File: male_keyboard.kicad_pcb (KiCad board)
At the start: 2 copper layers, 1 part, among them J1 Elite-Pi Microcontroller

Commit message: 1504202502
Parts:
- added J2: AudioJack4, Keebio-Parts:TRRS-PJ-320A, F.Cu at (34.8, 87.3)
- added SW1: SW_MEC_5G, Button_Switch_Keyboard:SW_Cherry_MX_1.00u_PCB, F.Cu at (101.5, 22.4)
- moved J1 36.6 mm to (64.5, 56.8)
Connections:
- J1 pad 19: unconnected-(J1-Pin_19-Pad19) -> Net-(J1-Pin_19)
- J1 pad 2: GND -> Net-(J1-Pin_2)
- J1 pad 21: unconnected-(J1-Pin_21-Pad21) -> Net-(J1-Pin_21)
- J1 pad 23: unconnected-(J1-Pin_23-Pad23) -> GND

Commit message: Label controller
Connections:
- net Net-(J1-Pin_21) renamed VCC
- J1 pad 1: unconnected-(J1-Pin_1-Pad1) -> 1
- J1 pad 10: unconnected-(J1-Pin_10-Pad10) -> 8
- J1 pad 11: unconnected-(J1-Pin_11-Pad11) -> 9
- J1 pad 12: unconnected-(J1-Pin_12-Pad12) -> 10
- J1 pad 13: unconnected-(J1-Pin_13-Pad13) -> 15
- J1 pad 14: unconnected-(J1-Pin_14-Pad14) -> 16
- J1 pad 15: unconnected-(J1-Pin_15-Pad15) -> 17
- J1 pad 16: unconnected-(J1-Pin_16-Pad16) -> 18
- J1 pad 19: Net-(J1-Pin_19) -> unconnected-(J1-Pin_19-Pad19)
- J1 pad 2: Net-(J1-Pin_2) -> 2
- J1 pad 25: unconnected-(J1-Pin_25-Pad25) -> 10
- J1 pad 26: unconnected-(J1-Pin_26-Pad26) -> 11
- J1 pad 27: unconnected-(J1-Pin_27-Pad27) -> 12
- J1 pad 28: unconnected-(J1-Pin_28-Pad28) -> 13
- J1 pad 29: unconnected-(J1-Pin_29-Pad29) -> 14
- J1 pad 3: unconnected-(J1-Pin_3-Pad3) -> GND
- J1 pad 4: unconnected-(J1-Pin_4-Pad4) -> GND
- J1 pad 5: unconnected-(J1-Pin_5-Pad5) -> 3
- J1 pad 6: unconnected-(J1-Pin_6-Pad6) -> 4
- J1 pad 7: unconnected-(J1-Pin_7-Pad7) -> 5
- J1 pad 8: unconnected-(J1-Pin_8-Pad8) -> 6
- J1 pad 9: unconnected-(J1-Pin_9-Pad9) -> 7
- J2 pad 3: Net-(J1-Pin_2) -> R1
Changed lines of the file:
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@@
 			(psa4output no)
 			(plot_black_and_white yes)
-			(plotinvisibletext no)
 			(sketchpadsonfab no)
 			(plotpadnumbers no)
@@
 	)
 	(net 0 "")
-	(net 1 "unconnected-(J1-Pin_6-Pad6)")
-	(net 2 "unconnected-(J1-Pin_15-Pad15)")
-	(net 3 "unconnected-(J1-Pin_26-Pad26)")
-	(net 4 "unconnected-(J1-Pin_28-Pad28)")
-	(net 5 "unconnected-(J1-Pin_13-Pad13)")
-	(net 6 "Net-(J1-Pin_21)")
-	(net 7 "unconnected-(J1-Pin_12-Pad12)")
-	(net 8 "unconnected-(J1-Pin_8-Pad8)")
+	(net 1 "4")
+	(net 2 "17")
+	(net 3 "11")
+	(net 4 "13")
+	(net 5 "15")
+	(net 6 "10")
+	(net 7 "6")
+	(net 8 "1")
 	(net 9 "unconnected-(J1-Pin_17-Pad17)")
-	(net 10 "unconnected-(J1-Pin_1-Pad1)")
-	(net 11 "unconnected-(J1-Pin_16-Pad16)")
-	(net 12 "unconnected-(J1-Pin_3-Pad3)")
-	(net 13 "unconnected-(J1-Pin_9-Pad9)")
-	(net 14 "unconnected-(J1-Pin_25-Pad25)")
-	(net 15 "Net-(J1-Pin_2)")
-	(net 16 "unconnected-(J1-Pin_5-Pad5)")
-	(net 17 "unconnected-(J1-Pin_14-Pad14)")
-	(net 18 "unconnected-(J1-Pin_11-Pad11)")
-	(net 19 "unconnected-(J1-Pin_7-Pad7)")
-	(net 20 "unconnected-(J1-Pin_10-Pad10)")
-	(net 21 "unconnected-(J1-Pin_4-Pad4)")
-	(net 22 "unconnected-(J1-Pin_29-Pad29)")
+	(net 10 "18")
+	(net 11 "7")
+	(net 12 "VCC")
+	(net 13 "3")
+	(net 14 "16")
+	(net 15 "9")
+	(net 16 "5")
+	(net 17 "8")
+	(net 18 "14")
+	(net 19 "2")
+	(net 20 "unconnected-(J1-Pin_19-Pad19)")
+	(net 21 "12")
+	(net 22 "R1")
 	(net 23 "unconnected-(J1-Pin_24-Pad24)")
 	(net 24 "unconnected-(J1-Pin_18-Pad18)")
@@
 	(net 26 "unconnected-(J1-Pin_20-Pad20)")
 	(net 27 "unconnected-(J1-Pin_22-Pad22)")
-	(net 28 "unconnected-(J1-Pin_27-Pad27)")
-	(net 29 "GND")
+	(net 28 "GND")
 	(footprint "Button_Switch_Keyboard:SW_Cherry_MX_1.00u_PCB"
 		(layer "F.Cu")
@@
 			(layers "*.Cu" "*.Mask")
 			(remove_unused_layers no)
-			(net 29 "GND")
+			(net 28 "GND")
 			(pinfunction "2")
 			(pintype "passive")
@@
 			(layers "*.Cu" "*.SilkS" "*.Mask")
 			(remove_unused_layers no)
-			(net 10 "unconnected-(J1-Pin_1-Pad1)")
+			(net 8 "1")
 			(pinfunction "Pin_1")
 			(pintype "passive")
@@
 			(layers "*.Cu" "*.SilkS" "*.Mask")
 			(remove_unused_layers no)
-			(net 15 "Net-(J1-Pin_2)")
+			(net 19 "2")
 			(pinfunction "Pin_2")
 			(pintype "passive")
@@
 			(layers "*.Cu" "*.SilkS" "*.Mask")
 			(remove_unused_layers no)
-			(net 12 "unconnected-(J1-Pin_3-Pad3)")
+			(net 28 "GND")
 			(pinfunction "Pin_3")
 			(pintype "passive")
@@
 			(layers "*.Cu" "*.SilkS" "*.Mask")
 			(remove_unused_layers no)
-			(net 21 "unconnected-(J1-Pin_4-Pad4)")
+			(net 28 "GND")
 			(pinfunction "Pin_4")
 			(pintype "passive")
@@
 			(layers "*.Cu" "*.SilkS" "*.Mask")
 			(remove_unused_layers no)
-			(net 16 "unconnected-(J1-Pin_5-Pad5)")
+			(net 13 "3")
 			(pinfunction "Pin_5")
 			(pintype "passive")
@@
 			(layers "*.Cu" "*.SilkS" "*.Mask")
 			(remove_unused_layers no)
-			(net 1 "unconnected-(J1-Pin_6-Pad6)")
+			(net 1 "4")
 			(pinfunction "Pin_6")
 			(pintype "passive")
@@
 			(layers "*.Cu" "*.SilkS" "*.Mask")
 			(remove_unused_layers no)
-			(net 19 "unconnected-(J1-Pin_7-Pad7)")
+			(net 16 "5")
 			(pinfunction "Pin_7")
 			(pintype "passive")
@@
 			(layers "*.Cu" "*.SilkS" "*.Mask")
 			(remove_unused_layers no)
-			(net 8 "unconnected-(J1-Pin_8-Pad8)")
+			(net 7 "6")
 			(pinfunction "Pin_8")
 			(pintype "passive")
@@
 			(layers "*.Cu" "*.SilkS" "*.Mask")
 			(remove_unused_layers no)
-			(net 13 "unconnected-(J1-Pin_9-Pad9)")
+			(net 11 "7")
 			(pinfunction "Pin_9")
 			(pintype "passive")
@@
 			(layers "*.Cu" "*.SilkS" "*.Mask")
 			(remove_unused_layers no)
-			(net 20 "unconnected-(J1-Pin_10-Pad10)")
+			(net 17 "8")
 			(pinfunction "Pin_10")
 			(pintype "passive")
@@
 			(layers "*.Cu" "*.SilkS" "*.Mask")
 			(remove_unused_layers no)
-			(net 18 "unconnected-(J1-Pin_11-Pad11)")
+			(net 15 "9")
 			(pinfunction "Pin_11")
 			(pintype "passive")
@@
 			(layers "*.Cu" "*.SilkS" "*.Mask")
 			(remove_unused_layers no)
-			(net 7 "unconnected-(J1-Pin_12-Pad12)")
+			(net 6 "10")
 			(pinfunction "Pin_12")
 			(pintype "passive")
@@
 			(layers "*.Cu" "*.SilkS" "*.Mask")
 			(remove_unused_layers no)
-			(net 5 "unconnected-(J1-Pin_13-Pad13)")
+			(net 5 "15")
 			(pinfunction "Pin_13")
 			(pintype "passive")
@@
 			(layers "*.Cu" "*.SilkS" "*.Mask")
 			(remove_unused_layers no)
-			(net 17 "unconnected-(J1-Pin_14-Pad14)")
+			(net 14 "16")
 			(pinfunction "Pin_14")
 			(pintype "passive")
@@
 			(layers "*.Cu" "*.SilkS" "*.Mask")
 			(remove_unused_layers no)
-			(net 2 "unconnected-(J1-Pin_15-Pad15)")
+			(net 2 "17")
 			(pinfunction "Pin_15")
 			(pintype "passive")
@@
 			(layers "*.Cu" "*.SilkS" "*.Mask")
 			(remove_unused_layers no)
-			(net 11 "unconnected-(J1-Pin_16-Pad16)")
+			(net 10 "18")
 			(pinfunction "Pin_16")
 			(pintype "passive")
@@
 			(layers "*.Cu" "*.SilkS" "*.Mask")
 			(remove_unused_layers no)
-			(net 25 "Net-(J1-Pin_19)")
+			(net 20 "unconnected-(J1-Pin_19-Pad19)")
 			(pinfunction "Pin_19")
 			(pintype "passive")
@@
 			(layers "*.Cu" "*.SilkS" "*.Mask")
 			(remove_unused_layers no)
-			(net 6 "Net-(J1-Pin_21)")
+			(net 12 "VCC")
 			(pinfunction "Pin_21")
 			(pintype "passive")
@@
 			(layers "*.Cu" "*.SilkS" "*.Mask")
 			(remove_unused_layers no)
-			(net 29 "GND")
+			(net 28 "GND")
 			(pinfunction "Pin_23")
 			(pintype "passive")
@@
 			(layers "*.Cu" "*.SilkS" "*.Mask")
 			(remove_unused_layers no)
-			(net 14 "unconnected-(J1-Pin_25-Pad25)")
+			(net 6 "10")
 			(pinfunction "Pin_25")
 			(pintype "passive")
@@
 			(layers "*.Cu" "*.SilkS" "*.Mask")
 			(remove_unused_layers no)
-			(net 3 "unconnected-(J1-Pin_26-Pad26)")
+			(net 3 "11")
 			(pinfunction "Pin_26")
 			(pintype "passive")
@@
 			(layers "*.Cu" "*.SilkS" "*.Mask")
 			(remove_unused_layers no)
-			(net 28 "unconnected-(J1-Pin_27-Pad27)")
+			(net 21 "12")
 			(pinfunction "Pin_27")
 			(pintype "passive")
@@
 			(layers "*.Cu" "*.SilkS" "*.Mask")
 			(remove_unused_layers no)
-			(net 4 "unconnected-(J1-Pin_28-Pad28)")
+			(net 4 "13")
 			(pinfunction "Pin_28")
 			(pintype "passive")
@@
 			(layers "*.Cu" "*.SilkS" "*.Mask")
 			(remove_unused_layers no)
-			(net 22 "unconnected-(J1-Pin_29-Pad29)")
+			(net 18 "14")
 			(pinfunction "Pin_29")
 			(pintype "passive")
@@
 			(layers "*.Cu" "*.Mask")
 			(remove_unused_layers no)
-			(net 29 "GND")
+			(net 28 "GND")
 			(pintype "passive")
 		)
@@
 			(layers "*.Cu" "*.Mask")
 			(remove_unused_layers no)
-			(net 29 "GND")
+			(net 28 "GND")
 			(pintype "passive")
 		)
@@
 			(layers "*.Cu" "*.Mask")
 			(remove_unused_layers no)
-			(net 15 "Net-(J1-Pin_2)")
+			(net 22 "R1")
 			(pintype "passive")
 		)
@@
 			(layers "*.Cu" "*.Mask")
 			(remove_unused_layers no)
-			(net 6 "Net-(J1-Pin_21)")
-			(pintype "passive")
-		)
+			(net 12 "VCC")
+			(pintype "passive")
+		)

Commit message: sort pcb
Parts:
- added J3: AudioJack4, Keebio-Parts:TRRS-PJ-320A, F.Cu at (160.9, 93.1)
- added J4: Elite-Pi Microcontroller, Keebio-Parts:Elite-C, F.Cu at (166.6, 70.9)
- added SW10: SW_Push, Button_Switch_Keyboard:SW_Cherry_MX_1.00u_PCB, F.Cu at (112.8, 81.5)
- added SW11: SW_Push, Button_Switch_Keyboard:SW_Cherry_MX_1.00u_PCB, F.Cu at (27.9, 103.0)
- added SW12: SW_Push, Button_Switch_Keyboard:SW_Cherry_MX_1.00u_PCB, F.Cu at (49.9, 103.0)
- added SW13: SW_Push, Button_Switch_Keyboard:SW_Cherry_MX_1.00u_PCB, F.Cu at (70.3, 103.0)
- added SW14: SW_Push, Button_Switch_Keyboard:SW_Cherry_MX_1.00u_PCB, F.Cu at (92.0, 105.0)
- added SW15: SW_Push, Button_Switch_Keyboard:SW_Cherry_MX_1.00u_PCB, F.Cu at (112.6, 104.9)
- added SW16: SW_Push, Button_Switch_Keyboard:SW_Cherry_MX_1.00u_PCB, F.Cu at (84.6, 130.4)
- added SW17: SW_Push, Button_Switch_Keyboard:SW_Cherry_MX_1.00u_PCB, F.Cu at (106.8, 130.5)
- added SW18: SW_Push, Button_Switch_Keyboard:SW_Cherry_MX_1.00u_PCB, F.Cu at (128.8, 141.5)
- added SW19: SW_Push, Button_Switch_Keyboard:SW_Cherry_MX_1.00u_PCB, F.Cu at (193.5, 57.5)
- added SW2: SW_Push, Button_Switch_Keyboard:SW_Cherry_MX_1.00u_PCB, F.Cu at (48.9, 57.0)
- added SW20: SW_Push, Button_Switch_Keyboard:SW_Cherry_MX_1.00u_PCB, F.Cu at (214.5, 57.5)
- added SW21: SW_Push, Button_Switch_Keyboard:SW_Cherry_MX_1.00u_PCB, F.Cu at (235.5, 57.4)
- added SW22: SW_Push, Button_Switch_Keyboard:SW_Cherry_MX_1.00u_PCB, F.Cu at (256.5, 57.5)
- added SW23: SW_Push, Button_Switch_Keyboard:SW_Cherry_MX_1.00u_PCB, F.Cu at (276.9, 57.5)
- added SW24: SW_Push, Button_Switch_Keyboard:SW_Cherry_MX_1.00u_PCB, F.Cu at (193.5, 79.5)
- added SW25: SW_Push, Button_Switch_Keyboard:SW_Cherry_MX_1.00u_PCB, F.Cu at (214.3, 79.5)
- added SW26: SW_Push, Button_Switch_Keyboard:SW_Cherry_MX_1.00u_PCB, F.Cu at (235.3, 79.5)
- added SW27: SW_Push, Button_Switch_Keyboard:SW_Cherry_MX_1.00u_PCB, F.Cu at (256.4, 79.5)
- added SW28: SW_Push, Button_Switch_Keyboard:SW_Cherry_MX_1.00u_PCB, F.Cu at (276.9, 79.5)
- added SW29: SW_Push, Button_Switch_Keyboard:SW_Cherry_MX_1.00u_PCB, F.Cu at (193.8, 102.0)
- added SW3: SW_Push, Button_Switch_Keyboard:SW_Cherry_MX_1.00u_PCB, F.Cu at (70.3, 57.0)
- added SW30: SW_Push, Button_Switch_Keyboard:SW_Cherry_MX_1.00u_PCB, F.Cu at (215.8, 102.0)
- added SW31: SW_Push, Button_Switch_Keyboard:SW_Cherry_MX_1.00u_PCB, F.Cu at (236.3, 102.0)
- added SW32: SW_Push, Button_Switch_Keyboard:SW_Cherry_MX_1.00u_PCB, F.Cu at (256.9, 102.0)
- added SW33: SW_Push, Button_Switch_Keyboard:SW_Cherry_MX_1.00u_PCB, F.Cu at (276.5, 102.5)
- added SW34: SW_Push, Button_Switch_Keyboard:SW_Cherry_MX_1.00u_PCB, F.Cu at (225.8, 125.0)
- added SW35: SW_Push, Button_Switch_Keyboard:SW_Cherry_MX_1.00u_PCB, F.Cu at (204.5, 125.0)
- added SW36: SW_Push, Button_Switch_Keyboard:SW_Cherry_MX_1.00u_PCB, F.Cu at (177.3, 141.5)
- added SW37: SW_Push, Button_Switch_Keyboard:SW_Cherry_MX_1.00u_PCB, F.Cu at (273.7, 153.4)
- added SW4: SW_Push, Button_Switch_Keyboard:SW_Cherry_MX_1.00u_PCB, F.Cu at (91.7, 57.0)
- added SW5: SW_Push, Button_Switch_Keyboard:SW_Cherry_MX_1.00u_PCB, F.Cu at (112.8, 57.5)
- added SW6: SW_Push, Button_Switch_Keyboard:SW_Cherry_MX_1.00u_PCB, F.Cu at (27.9, 80.0)
- added SW7: SW_Push, Button_Switch_Keyboard:SW_Cherry_MX_1.00u_PCB, F.Cu at (48.9, 80.0)
- added SW8: SW_Push, Button_Switch_Keyboard:SW_Cherry_MX_1.00u_PCB, F.Cu at (70.0, 81.4)
- added SW9: SW_Push, Button_Switch_Keyboard:SW_Cherry_MX_1.00u_PCB, F.Cu at (91.8, 81.5)
- moved J2 102.0 mm to (136.7, 92.2), turned to -90 degrees
- moved SW1 81.3 mm to (27.9, 57.0)
- moved J1 68.0 mm to (131.0, 71.0)

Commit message: fix number of switches and positions
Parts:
- removed SW1: SW_MEC_5G, Button_Switch_Keyboard:SW_Cherry_MX_1.00u_PCB
- moved SW19 104.7 mm to (126.5, 137.9)
- moved SW37 97.1 mm to (177.8, 138.0)
- moved SW11 87.2 mm to (112.5, 81.9)
- moved SW6 86.7 mm to (112.0, 58.9)
- moved SW29 83.4 mm to (274.5, 80.4)
- moved SW24 83.3 mm to (274.0, 58.0)
- moved SW34 53.0 mm to (274.0, 103.0)
- moved SW16 37.8 mm to (112.5, 104.9)
- moved SW36 28.9 mm to (201.5, 125.5)
- moved SW18 28.6 mm to (103.0, 129.4)
- moved SW17 24.4 mm to (82.5, 129.5)
- moved SW32 24.3 mm to (232.5, 102.4)
- moved SW30 24.3 mm to (191.5, 102.4)
- moved SW31 24.3 mm to (212.0, 102.4)
- moved SW33 24.3 mm to (252.2, 103.0)
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
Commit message: 01052025
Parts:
- moved SW33 1.87 mm to (254.0, 102.5)
- moved SW34 0.71 mm to (274.5, 102.5)
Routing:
- net GND: track 0.00 -> 764.6 mm
- net 13: track 0.00 -> 176.1 mm
- net 12: track 0.00 -> 166.8 mm
- net 7: track 0.00 -> 97.0 mm
- net 1: track 0.00 -> 96.7 mm
- net 8: track 0.00 -> 77.9 mm
- net 2: track 0.00 -> 75.9 mm
- net 14: track 0.00 -> 74.9 mm
- net 17: track 0.00 -> 74.0 mm
- net 18: track 0.00 -> 68.6 mm
- net 15: track 0.00 -> 60.0 mm
- net 3: track 0.00 -> 57.5 mm
- net 10: track 0.00 -> 41.7 mm
- net 16: track 0.00 -> 36.6 mm
- net 4: track 0.00 -> 36.3 mm
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
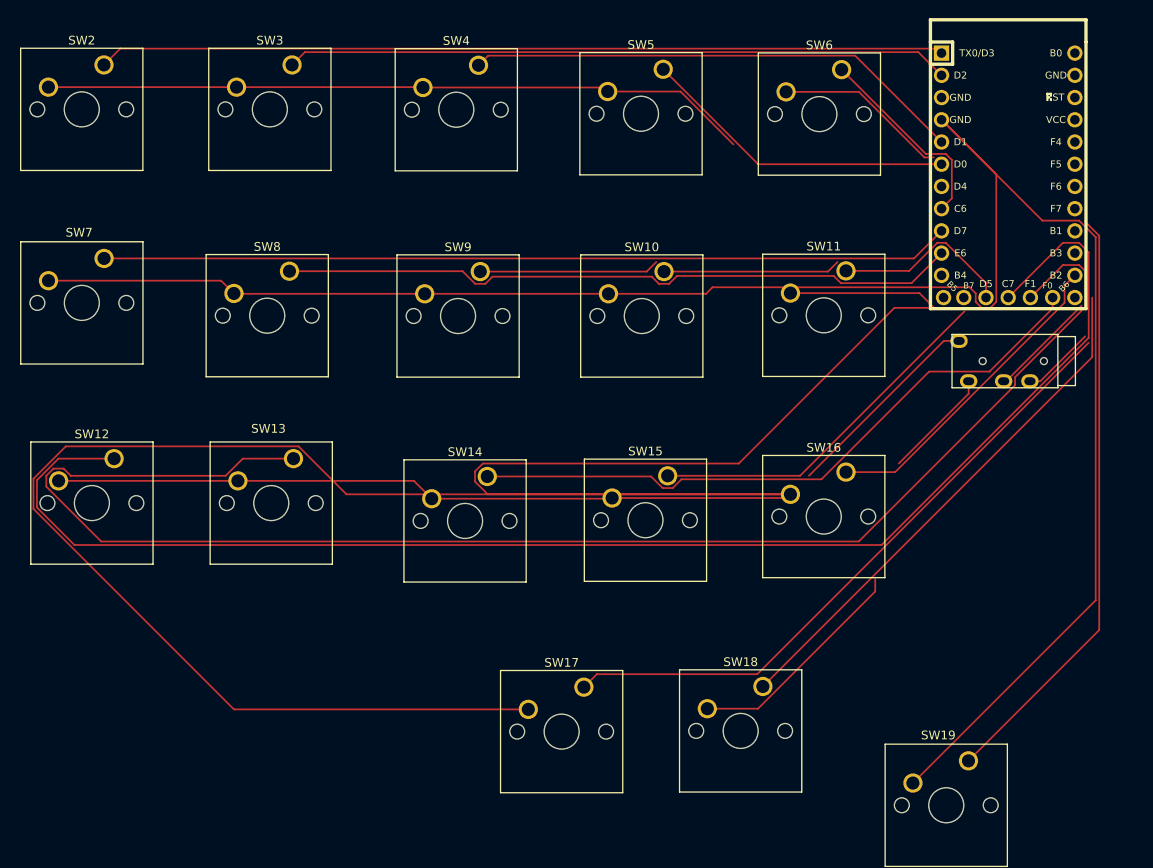
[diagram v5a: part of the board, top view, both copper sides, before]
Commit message: fix left side references
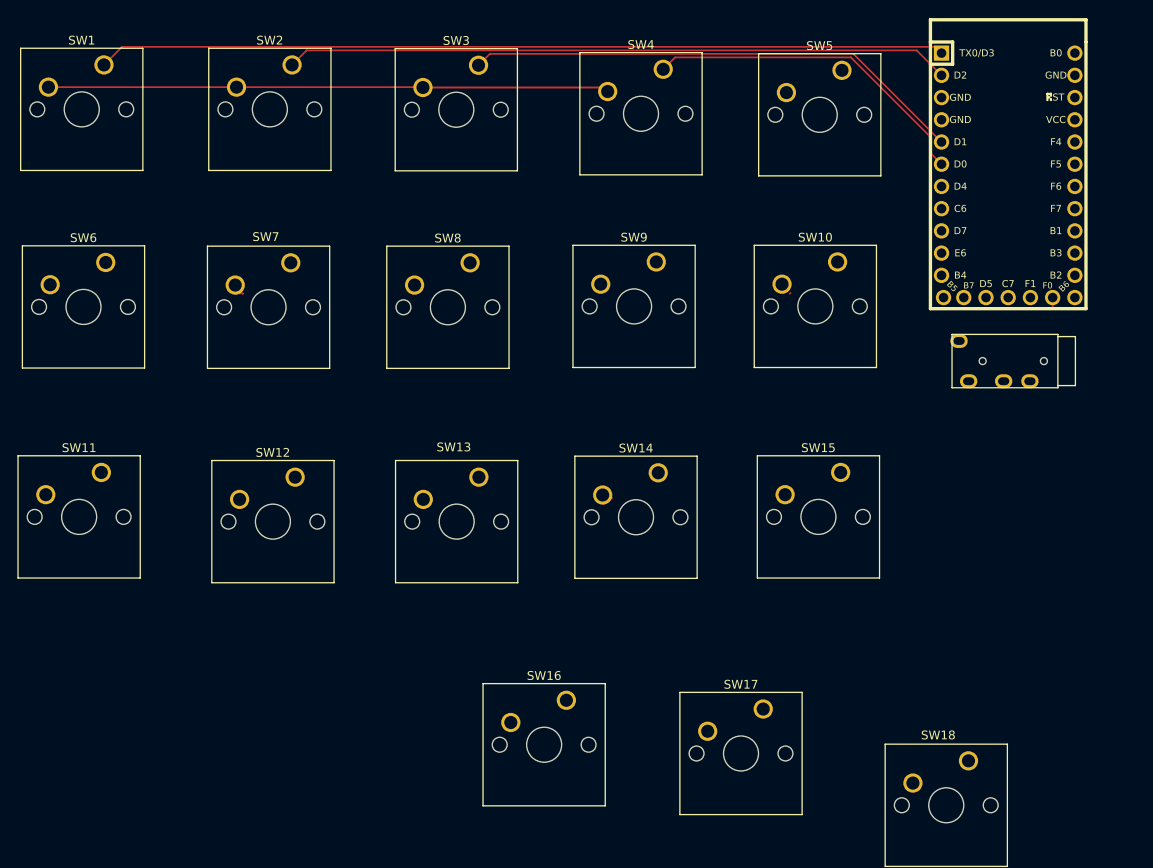
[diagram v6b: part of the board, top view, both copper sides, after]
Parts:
- moved SW11 88.2 mm to (27.4, 105.0)
- moved SW6 86.9 mm to (27.9, 81.0)
- moved SW16 41.3 mm to (80.5, 131.0)
- moved SW10 31.2 mm to (111.5, 80.9)
- moved SW5 30.7 mm to (112.0, 59.0)
- moved SW15 26.0 mm to (111.8, 105.0)
- moved SW7 21.3 mm to (49.0, 81.0)
- moved SW13 21.3 mm to (70.5, 105.5)
- moved SW12 20.8 mm to (49.5, 105.5)
- moved SW8 20.7 mm to (69.5, 81.0)
- moved SW17 20.7 mm to (103.0, 132.0)
- moved SW9 20.1 mm to (90.8, 80.9)
- moved SW14 19.5 mm to (91.0, 105.0)
- renumbered SW2 to SW1, SW15 to SW10, SW18 to SW15, SW19 to SW18, SW3 to SW2, SW4 to SW3, SW5 to SW4, SW10 to SW5
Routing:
- net GND: track 764.6 -> 65.5 mm
- net 13: track 176.1 -> 0.00 mm
- net 12: track 166.8 -> 0.00 mm
- net 7: track 97.0 -> 0.00 mm
- net 8: track 77.9 -> 0.00 mm
- net 17: track 74.0 -> 0.00 mm
- net 14: track 74.9 -> 1.24 mm
- net 18: track 68.6 -> 0.00 mm
- net 15: track 60.0 -> 0.00 mm
- net 10: track 41.7 -> 0.00 mm
- net 16: track 36.6 -> 0.00 mm
- net 6: track 22.9 -> 0.00 mm
- net 11: track 20.9 -> 0.00 mm
- net 9: track 20.6 -> 0.00 mm
- net 5: track 20.3 -> 0.00 mm
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
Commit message: merge and some more updates
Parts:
- renumbered SW20 to SW19, SW21 to SW20, SW22 to SW21, SW23 to SW22, SW28 to SW23, SW33 to SW28, SW37 to SW33
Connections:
- net 3a renamed 21
- net 8a renamed 26
- J1 pad 13: 15 -> 16
- J1 pad 14: 16 -> 17
- J1 pad 15: 17 -> 18
- J1 pad 16: 18 -> unconnected-(J1-Pin_16-Pad16)
- J1 pad 25: 10 -> 11
- J1 pad 26: 11 -> 12
- J1 pad 27: 12 -> 13
- J1 pad 28: 13 -> 14
- J1 pad 29: 14 -> 15
- J4 pad 1: 1a -> 19
- J4 pad 11: 9a -> 27
- J4 pad 12: 10a -> 28
- J4 pad 13: 15a -> 34
- J4 pad 14: 16a -> 35
- J4 pad 15: 17a -> 36
- J4 pad 16: 18a -> unconnected-(J4-Pin_16-Pad16)
- J4 pad 2: 2a -> 20
- J4 pad 25: 10a -> 29
- J4 pad 26: 11a -> 30
- J4 pad 27: 12a -> 31
- J4 pad 28: 13a -> 32
- J4 pad 29: 14a -> 33
- J4 pad 6: 4a -> 22
- J4 pad 7: 20 -> 23
- J4 pad 8: 6a -> 24
- J4 pad 9: 7a -> 25
- SW19 pad 1: 20 -> 19
- SW20 pad 1: 4a -> 20
- SW22 pad 1: 2a -> 22
- SW23 pad 1: 1a -> 23
- SW24 pad 1: 10a -> 24
- SW25 pad 1: 9a -> 25
- SW27 pad 1: 7a -> 27
- SW28 pad 1: 6a -> 28
- SW29 pad 1: 15a -> 29
- SW30 pad 1: 14a -> 30
- SW31 pad 1: 13a -> 31
- SW32 pad 1: 12a -> 32
- SW33 pad 1: 11a -> 33
- SW34 pad 1: 18a -> 34
- SW35 pad 1: 17a -> 35
- SW36 pad 1: 16a -> 36
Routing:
- net 15: track 0.00 -> 1.24 mm
- net 14: track 1.24 -> 0.00 mm
